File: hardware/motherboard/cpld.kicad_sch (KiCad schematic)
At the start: 1 part, among them U26 ATF1508AS-10AU100

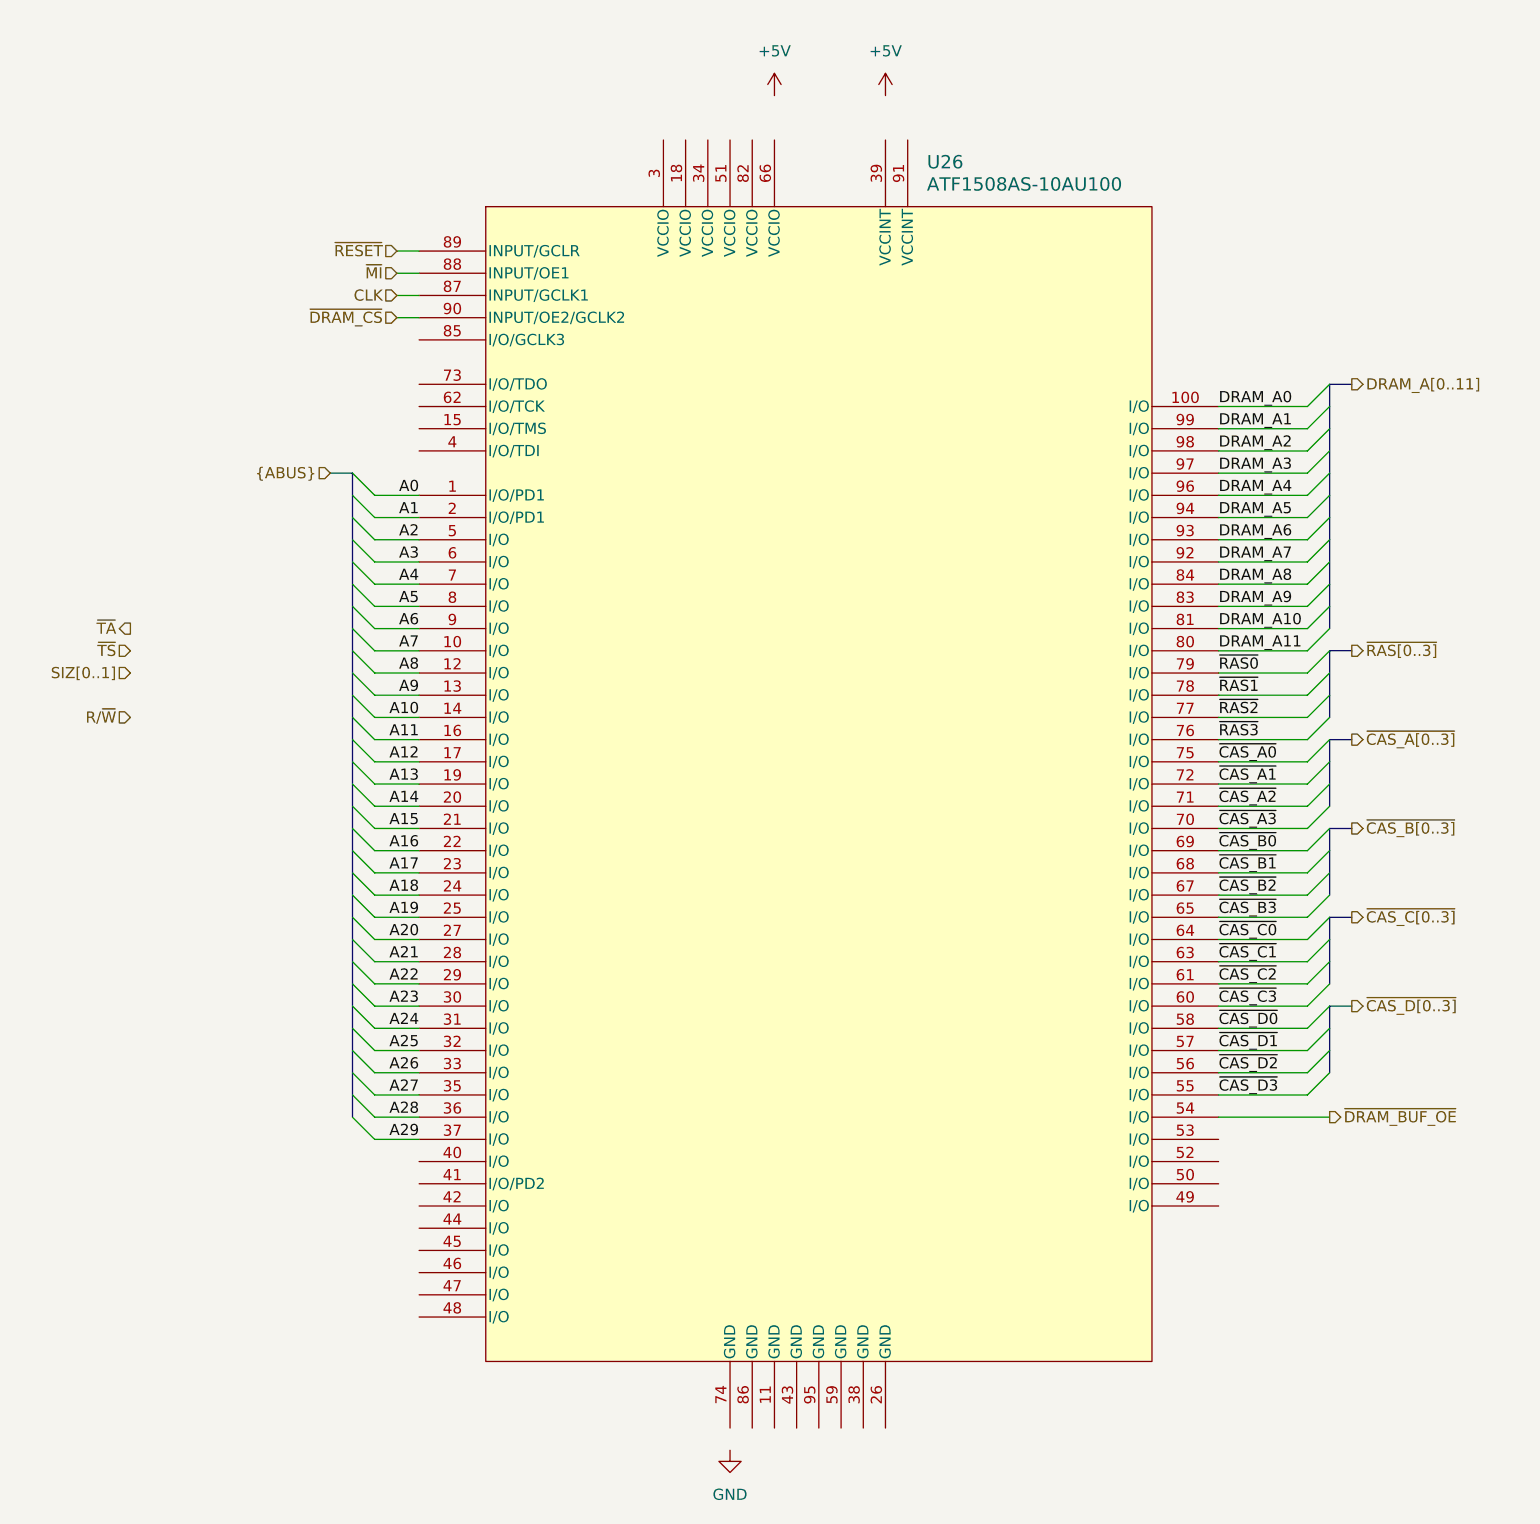
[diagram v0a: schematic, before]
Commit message: restructure, create minimum board project
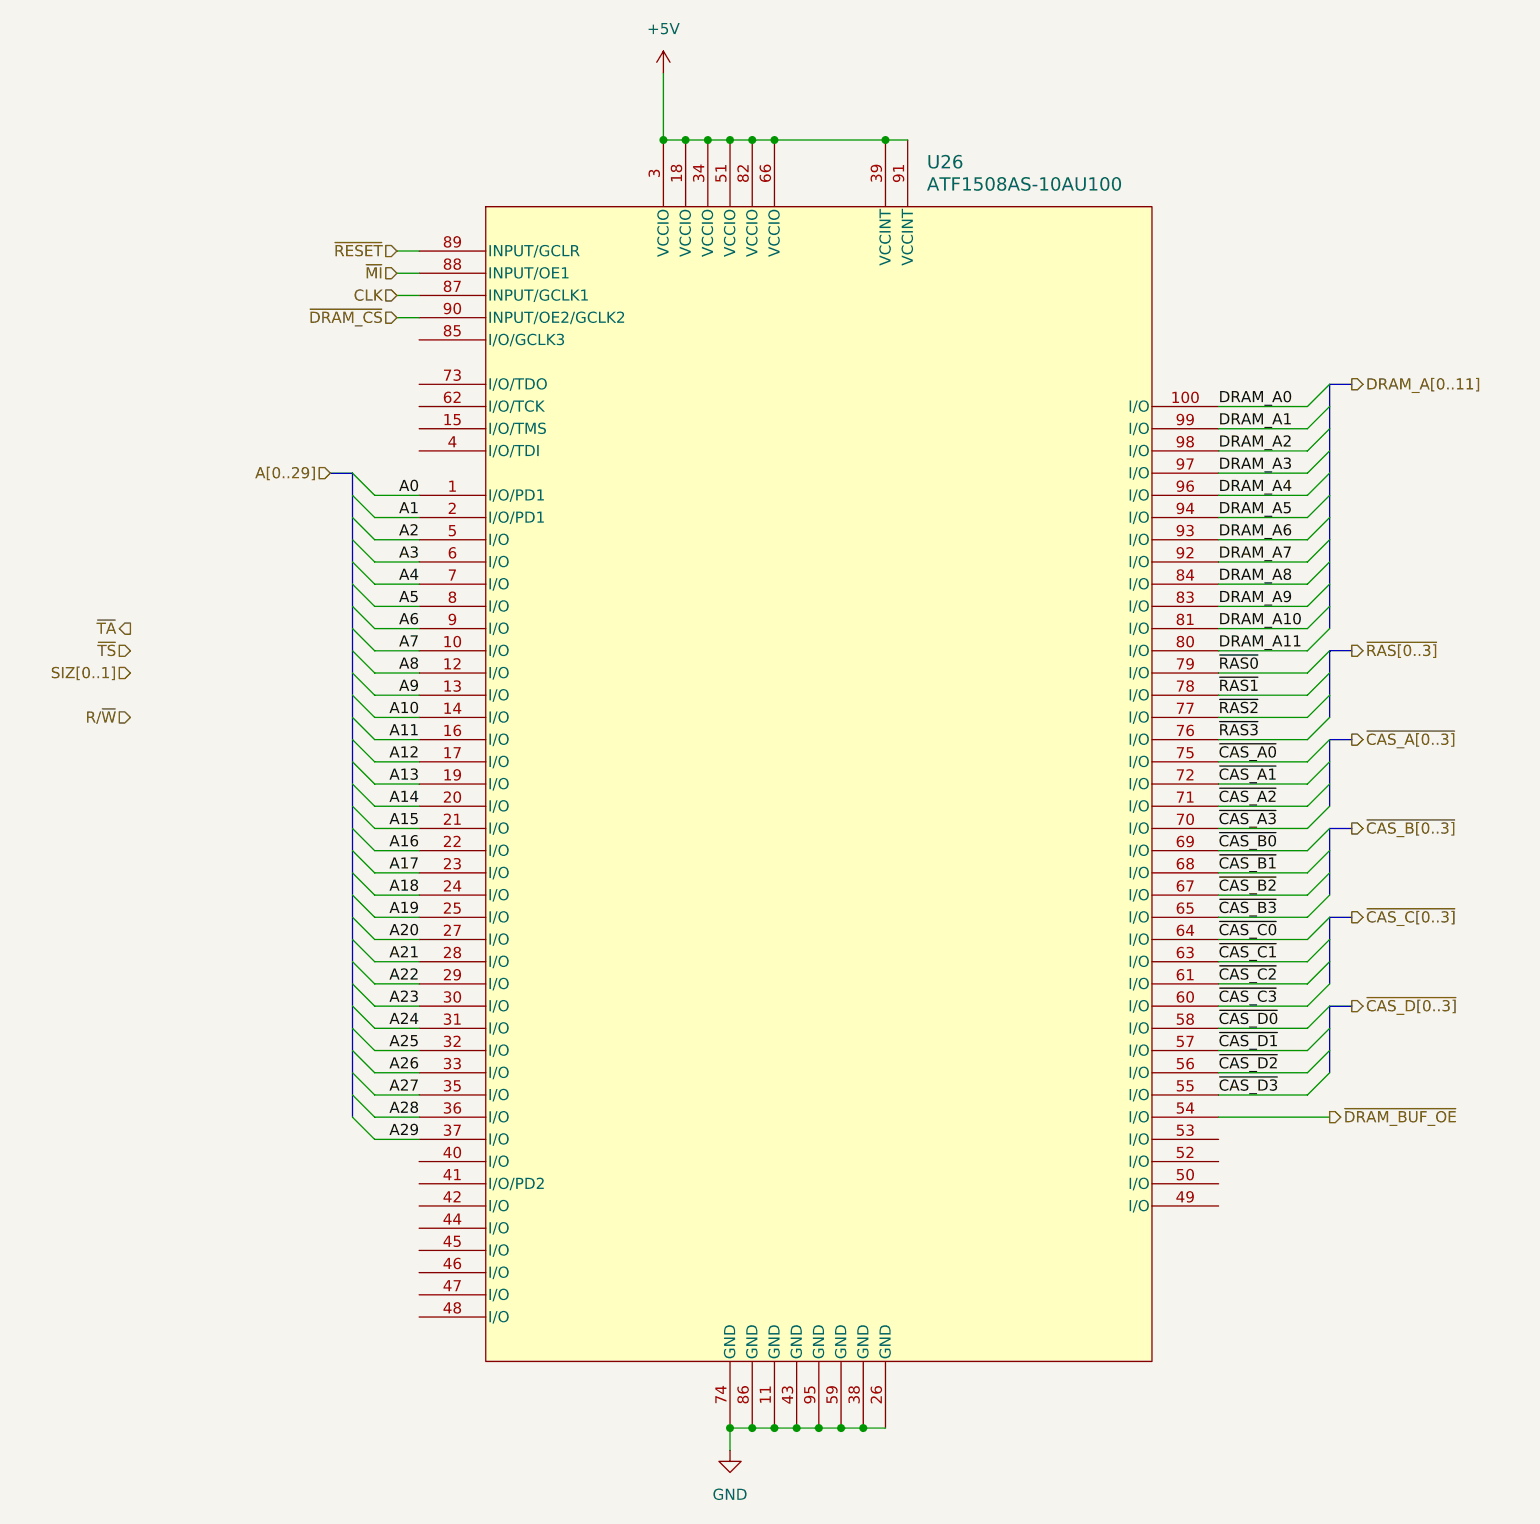
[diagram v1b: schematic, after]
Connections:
- net +5V: now also U26.18 (VCCIO), U26.3 (VCCIO), U26.34 (VCCIO), U26.39 (VCCINT), U26.51 (VCCIO), U26.66 (VCCIO), U26.82 (VCCIO), U26.91 (VCCINT)
- net GND: now also U26.11 (GND), U26.26 (GND), U26.38 (GND), U26.43 (GND), U26.59 (GND), U26.74 (GND), U26.86 (GND), U26.95 (GND)
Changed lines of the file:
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@@
 (kicad_sch (version 20230121) (generator eeschema)
   (paper "A4")
+  (junction (at 101.6 180.34) (diameter 0) (color 0 0 0 0)
+  )
+  (junction (at 93.98 33.02) (diameter 0) (color 0 0 0 0)
+  )
+  (junction (at 111.76 180.34) (diameter 0) (color 0 0 0 0)
+  )
+  (junction (at 96.52 33.02) (diameter 0) (color 0 0 0 0)
+  )
+  (junction (at 91.44 33.02) (diameter 0) (color 0 0 0 0)
+  )
+  (junction (at 104.14 33.02) (diameter 0) (color 0 0 0 0)
+  )
+  (junction (at 106.68 180.34) (diameter 0) (color 0 0 0 0)
+  )
+  (junction (at 114.3 180.34) (diameter 0) (color 0 0 0 0)
+  )
+  (junction (at 104.14 180.34) (diameter 0) (color 0 0 0 0)
+  )
+  (junction (at 116.84 33.02) (diameter 0) (color 0 0 0 0)
+  )
+  (junction (at 99.06 180.34) (diameter 0) (color 0 0 0 0)
+  )
+  (junction (at 109.22 180.34) (diameter 0) (color 0 0 0 0)
+  )
+  (junction (at 101.6 33.02) (diameter 0) (color 0 0 0 0)
+  )
+  (junction (at 99.06 33.02) (diameter 0) (color 0 0 0 0)
+  )
   (bus_entry (at 167.64 76.2) (size -2.54 2.54)
     (stroke (width 0) (type default))
@@
     (stroke (width 0) (type default))
   )
+  (wire (pts (xy 93.98 33.02) (xy 96.52 33.02))
+    (stroke (width 0) (type default))
+  )
+  (wire (pts (xy 99.06 180.34) (xy 101.6 180.34))
+    (stroke (width 0) (type default))
+  )
   (wire (pts (xy 154.94 139.7) (xy 165.1 139.7))
     (stroke (width 0) (type default))
@@
     (stroke (width 0) (type default))
   )
+  (wire (pts (xy 96.52 33.02) (xy 99.06 33.02))
+    (stroke (width 0) (type default))
+  )
   (wire (pts (xy 58.42 99.06) (xy 63.5 99.06))
     (stroke (width 0) (type default))
@@
     (stroke (width 0) (type default))
   )
+  (wire (pts (xy 104.14 180.34) (xy 106.68 180.34))
+    (stroke (width 0) (type default))
+  )
   (wire (pts (xy 58.42 73.66) (xy 63.5 73.66))
     (stroke (width 0) (type default))
@@
     (stroke (width 0) (type default))
   )
+  (wire (pts (xy 106.68 180.34) (xy 109.22 180.34))
+    (stroke (width 0) (type default))
+  )
   (bus (pts (xy 55.88 91.44) (xy 55.88 93.98))
     (stroke (width 0) (type default))
   )
+  (wire (pts (xy 116.84 33.02) (xy 119.38 33.02))
+    (stroke (width 0) (type default))
+  )
   (bus (pts (xy 55.88 86.36) (xy 55.88 88.9))
     (stroke (width 0) (type default))
@@
     (stroke (width 0) (type default))
   )
+  (wire (pts (xy 101.6 33.02) (xy 104.14 33.02))
+    (stroke (width 0) (type default))
+  )
   (wire (pts (xy 58.42 142.24) (xy 63.5 142.24))
     (stroke (width 0) (type default))
@@
     (stroke (width 0) (type default))
   )
+  (wire (pts (xy 101.6 180.34) (xy 104.14 180.34))
+    (stroke (width 0) (type default))
+  )
   (wire (pts (xy 58.42 119.38) (xy 63.5 119.38))
     (stroke (width 0) (type default))
@@
     (stroke (width 0) (type default))
   )
+  (wire (pts (xy 109.22 180.34) (xy 111.76 180.34))
+    (stroke (width 0) (type default))
+  )
   (bus (pts (xy 167.64 111.76) (xy 167.64 114.3))
     (stroke (width 0) (type default))
@@
     (stroke (width 0) (type default))
   )
+  (wire (pts (xy 114.3 180.34) (xy 116.84 180.34))
+    (stroke (width 0) (type default))
+  )
   (bus (pts (xy 167.64 124.46) (xy 167.64 127))
     (stroke (width 0) (type default))
@@
     (stroke (width 0) (type default))
   )
+  (wire (pts (xy 91.44 33.02) (xy 93.98 33.02))
+    (stroke (width 0) (type default))
+  )
   (bus (pts (xy 167.64 71.12) (xy 167.64 73.66))
     (stroke (width 0) (type default))
@@
     (stroke (width 0) (type default))
   )
+  (wire (pts (xy 99.06 33.02) (xy 101.6 33.02))
+    (stroke (width 0) (type default))
+  )
   (wire (pts (xy 154.94 124.46) (xy 165.1 124.46))
     (stroke (width 0) (type default))
@@
     (stroke (width 0) (type default))
   )
+  (wire (pts (xy 99.06 182.88) (xy 99.06 180.34))
+    (stroke (width 0) (type default))
+  )
   (bus (pts (xy 55.88 101.6) (xy 55.88 104.14))
     (stroke (width 0) (type default))
@@
     (stroke (width 0) (type default))
   )
+  (wire (pts (xy 104.14 33.02) (xy 116.84 33.02))
+    (stroke (width 0) (type default))
+  )
   (bus (pts (xy 167.64 63.5) (xy 167.64 66.04))
     (stroke (width 0) (type default))
@@
     (stroke (width 0) (type default))
   )
+  (wire (pts (xy 111.76 180.34) (xy 114.3 180.34))
+    (stroke (width 0) (type default))
+  )
   (bus (pts (xy 55.88 116.84) (xy 55.88 119.38))
     (stroke (width 0) (type default))
@@
   )
   (bus (pts (xy 55.88 78.74) (xy 55.88 81.28))
+    (stroke (width 0) (type default))
+  )
+  (wire (pts (xy 91.44 25.4) (xy 91.44 33.02))
     (stroke (width 0) (type default))
   )
@@
     (effects (font (size 1.27 1.27)) (justify left))
   )
-  (hierarchical_label "{ABUS}" (shape input) (at 53.34 71.12 180) (fields_autoplaced)
+  (hierarchical_label "A[0..29]" (shape input) (at 53.34 71.12 180) (fields_autoplaced)
     (effects (font (size 1.27 1.27)) (justify right))
   )
@@
     )
   )
-  (symbol (lib_id "power:+5V") (at 116.84 27.94 0) (unit 1)
+  (symbol (lib_id "power:+5V") (at 91.44 25.4 0) (unit 1)
     (in_bom yes) (on_board yes) (dnp no) (fields_autoplaced)
-    (property "Reference" "#PWR0114" (at 116.84 31.75 0)
+    (property "Reference" "#PWR0111" (at 91.44 29.21 0)
       (effects (font (size 1.27 1.27)) hide)
     )
-    (property "Value" "+5V" (at 116.84 22.86 0)
+    (property "Value" "+5V" (at 91.44 20.32 0)
       (effects (font (size 1.27 1.27)))
     )
-    (property "Footprint" "" (at 116.84 27.94 0)
+    (property "Footprint" "" (at 91.44 25.4 0)
       (effects (font (size 1.27 1.27)) hide)
     )
-    (property "Datasheet" "" (at 116.84 27.94 0)
+    (property "Datasheet" "" (at 91.44 25.4 0)
       (effects (font (size 1.27 1.27)) hide)
     )
-    (pin "1")
-    (instances
-      (project "68040pc"
-        (path "/3006deba-2100-40f8-9f39-987a5c2c14c7/4f6064b8-149d-4ca5-a87e-2a70892ab2ac"
-          (reference "#PWR0114") (unit 1)
-        )
-      )
-    )
-  )
-  (symbol (lib_id "power:+5V") (at 104.14 27.94 0) (unit 1)
-    (in_bom yes) (on_board yes) (dnp no) (fields_autoplaced)
-    (property "Reference" "#PWR0111" (at 104.14 31.75 0)
-      (effects (font (size 1.27 1.27)) hide)
-    )
-    (property "Value" "+5V" (at 104.14 22.86 0)
-      (effects (font (size 1.27 1.27)))
-    )
-    (property "Footprint" "" (at 104.14 27.94 0)
-      (effects (font (size 1.27 1.27)) hide)
-    )
-    (property "Datasheet" "" (at 104.14 27.94 0)
-      (effects (font (size 1.27 1.27)) hide)
-    )
